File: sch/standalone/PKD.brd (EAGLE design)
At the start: 61.9 x 67.8 mm, 30 parts, among them IC1 LM393N, IC2 TL084P, IC3 PIC12F683P, IC4 74HC244N, Q1 BS170

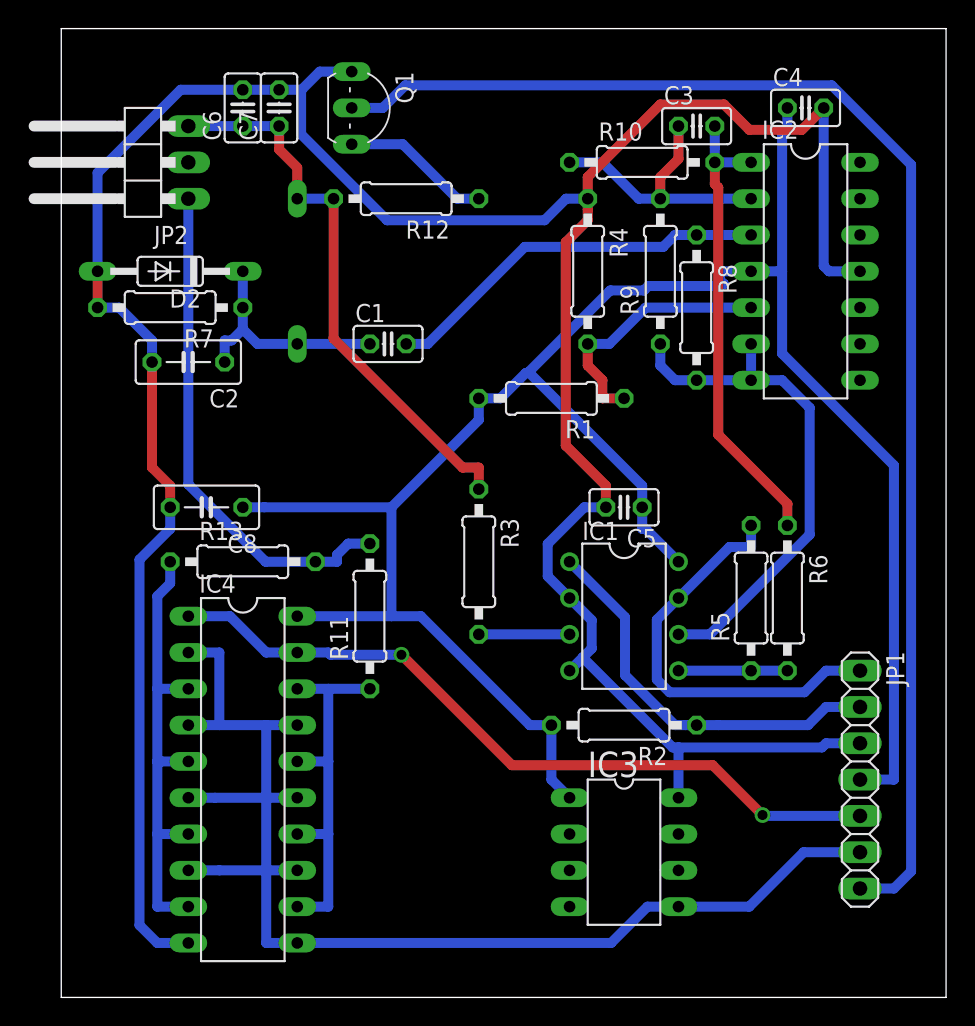
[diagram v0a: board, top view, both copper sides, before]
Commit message: Reader + emulator working, modified (reduced) schematics for standalone ver
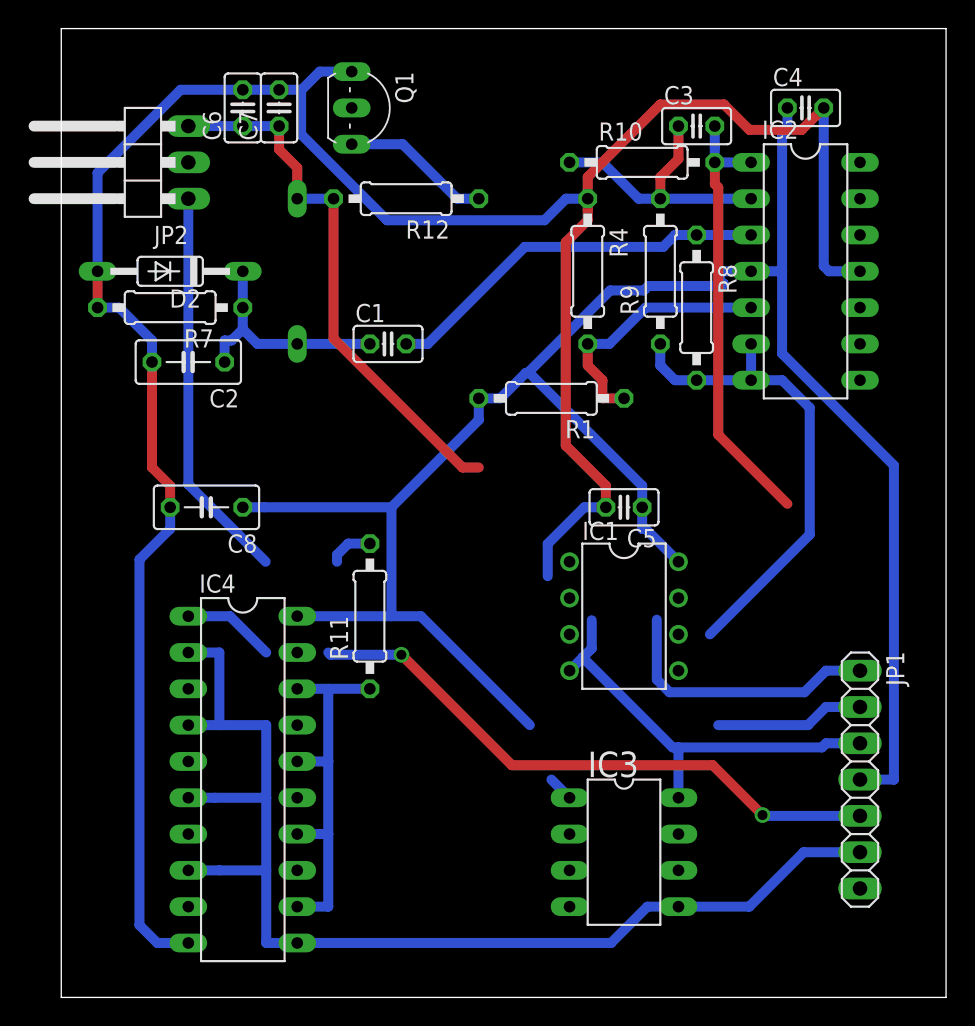
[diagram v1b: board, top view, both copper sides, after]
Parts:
- removed R13: 33, rcl:0207/10
- removed R2, R5: 10k, rcl:0207/10
- removed R3: 240k, rcl:0207/10
- removed R6: 2,2k, rcl:0207/10
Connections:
- removed net CROSS_LO: IC1.1, IC3.2, JP1.2, R2.1
- removed net LO_LOAD: JP1.7, Q1.2
- removed net LO_PKD_U: C3.2, IC2.1, R10.2, R6.1
- removed net N$15: IC4.3, IC4.5, IC4.7, IC4.9, R13.1
- removed net N$17: IC1.5, R5.1, R6.2
- removed net N$6: IC1.3, R3.2
- removed net PWR_OE1: IC4.1, IC4.19, JP1.5
- new net EMU_NOE: IC4.19
- new net GEN_NOE: IC4.1, JP1.5
- new net N$7: IC4.9, Q1.2
- net ANT_LO: no longer R3.1
- net GND: no longer IC1.2
- net LO_PKD: now also C3.2, IC2.1, R10.2; no longer IC1.7, R5.2
- net N$13: no longer R13.2
- net OCLK: now also IC3.2, JP1.2; no longer IC3.6
- net PWR_LO: no longer IC4.13, IC4.15, IC4.17
- net VCC: no longer R2.2
- net VMID: no longer IC1.6
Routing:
- net LO_LOAD: track 95.6 -> 0.00 mm
- net PWR_OE1: track 52.8 -> 0.00 mm, vias 2 -> 0
- net GEN_NOE: track 0.00 -> 48.4 mm, vias 0 -> 2
- net N$15: track 33.2 -> 0.00 mm
- net LO_PKD_U: track 32.6 -> 0.00 mm
- net CROSS_LO: track 28.0 -> 0.00 mm
- net LO_PKD: track 29.6 -> 50.5 mm
- net OCLK: track 0.00 -> 10.4 mm
- net N$17: track 7.62 -> 0.00 mm
- net PWR_LO: track 89.5 -> 83.0 mm
- net N$6: track 6.35 -> 0.00 mm
- net VCC: track 151.0 -> 145.7 mm
- net N$13: track 35.7 -> 30.7 mm
- net GND: track 207.6 -> 203.3 mm
- net VMID: track 36.7 -> 34.5 mm
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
